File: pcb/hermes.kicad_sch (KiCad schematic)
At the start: 11 parts, among them J1 OLED_128x64, U1 XIAO-RP2040-DIP, U2 MAX30102

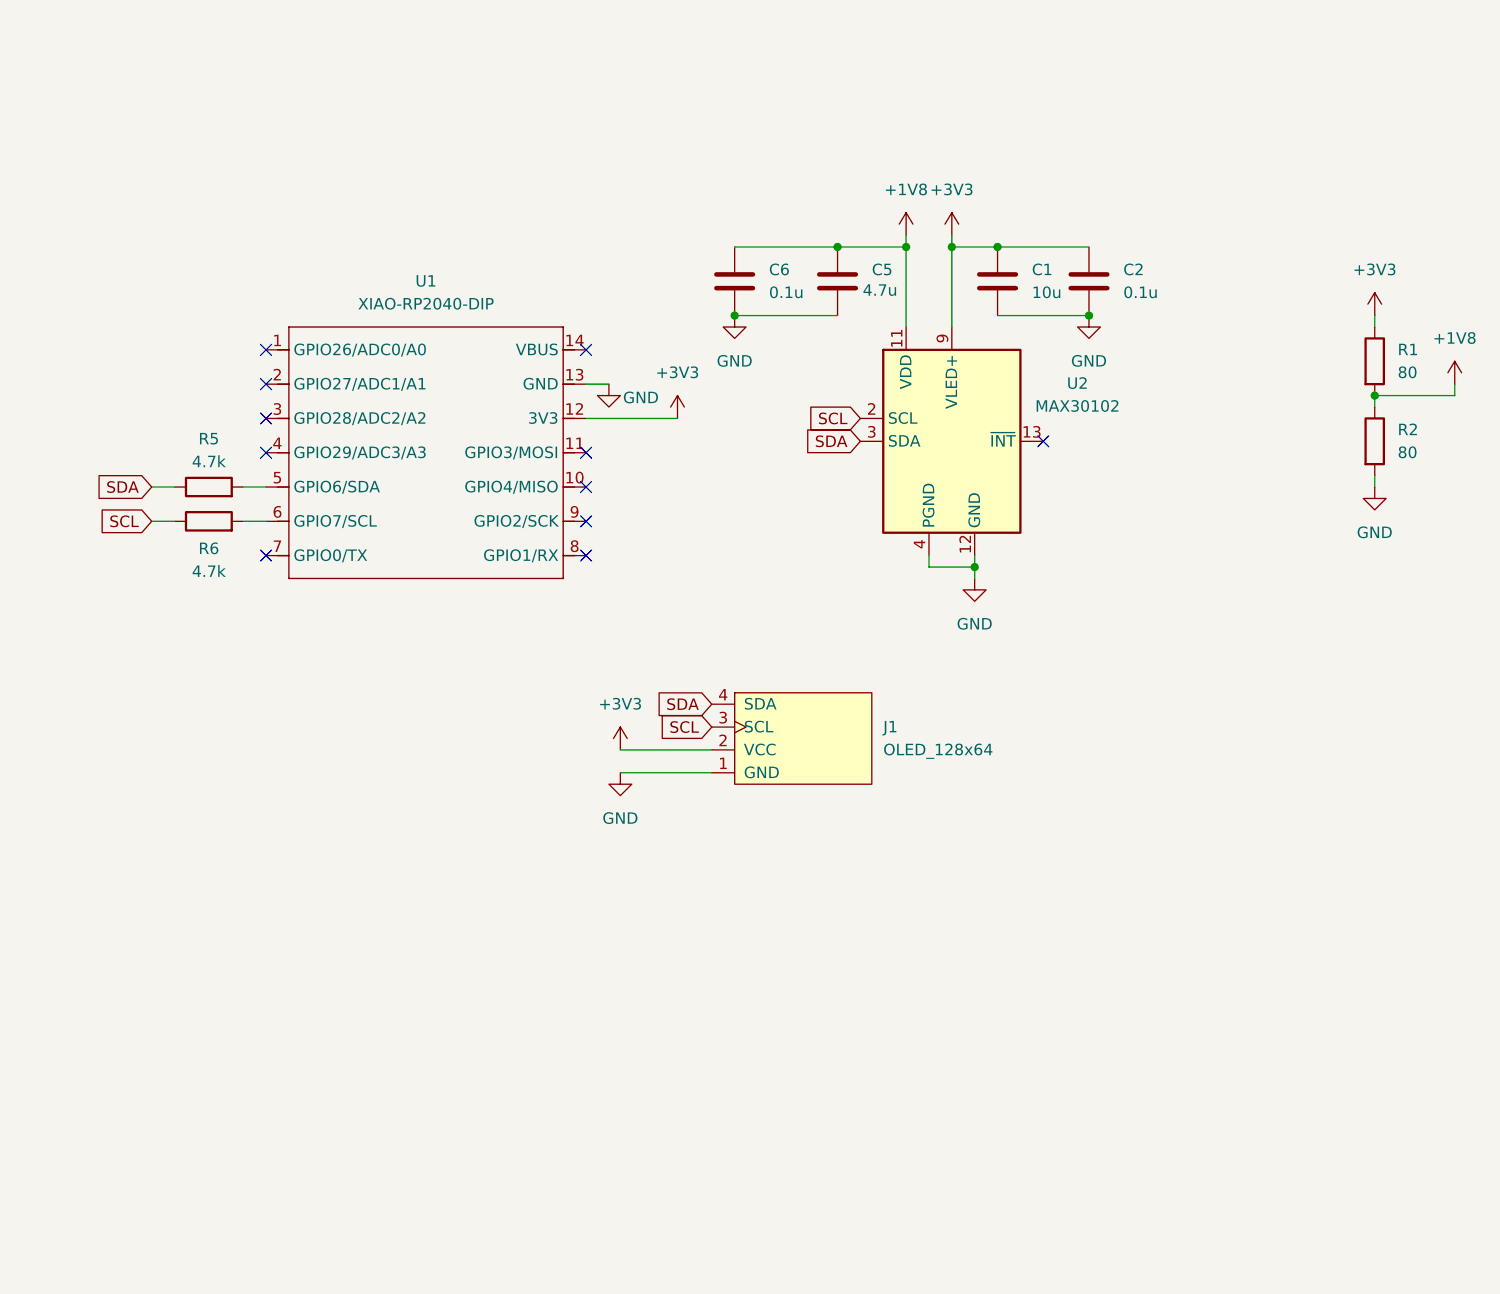
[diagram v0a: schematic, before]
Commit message: reroute board to incorporate TOF sensor
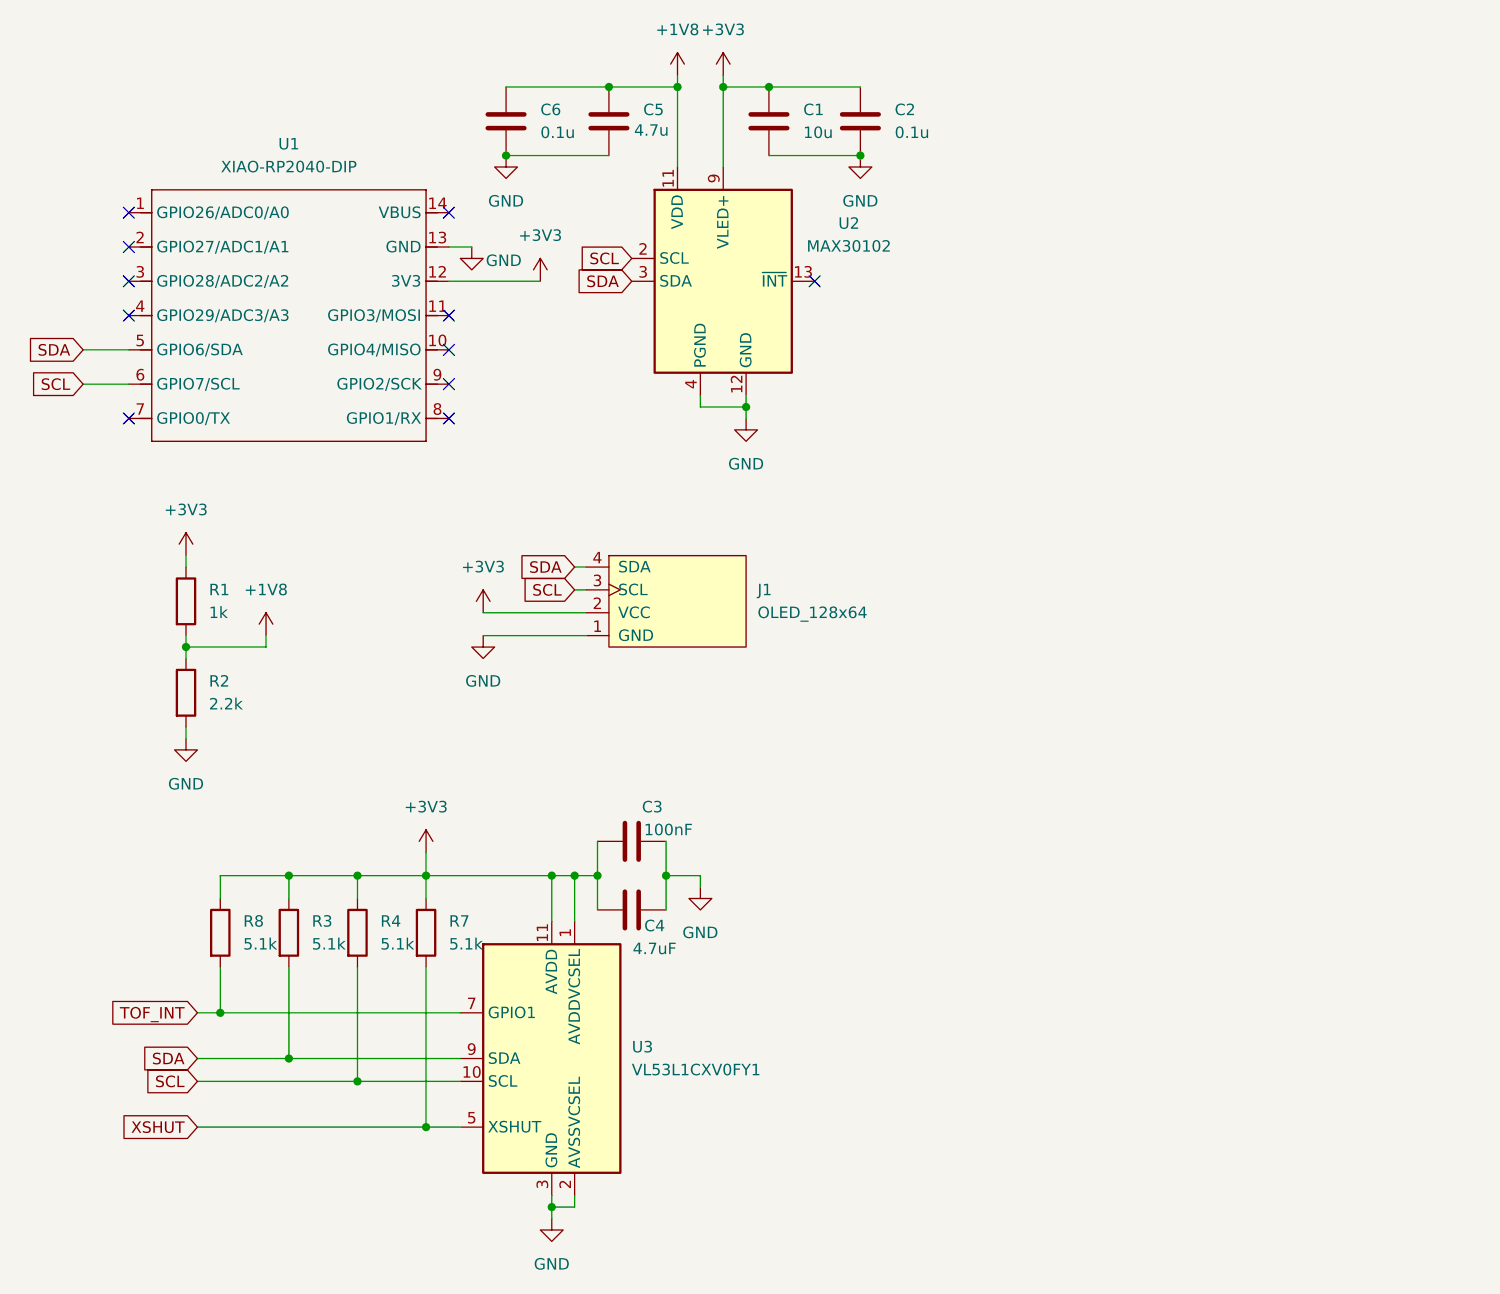
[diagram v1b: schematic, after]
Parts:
- removed R5, R6: 4.7k, Resistor_SMD:R_0805_2012Metric, symbol Device:R
- added C3: 100nF, Capacitor_SMD:C_0805_2012Metric, symbol Device:C
- added C4: 4.7uF, Capacitor_SMD:C_0805_2012Metric, symbol Device:C
- added R3, R4, R7, R8: 5.1k, Resistor_SMD:R_0805_2012Metric, symbol Device:R
- added U3: VL53L1CXV0FY1, Sensor_Distance:ST_VL53L1x, symbol Sensor_Distance:VL53L1CXV0FY1
- R1: value 80 -> 1k
- R2: value 80 -> 2.2k
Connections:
- net +3V3: now also C3.1, C4.1, R3.1, R4.1, R7.1, R8.1, U3.1 (AVDDVCSEL), U3.11 (AVDD)
- net GND: now also C3.2, C4.2, U3.12 (GND), U3.2 (AVSSVCSEL), U3.3 (GND), U3.4 (GND), U3.6 (GND)
- net SCL: now also U1.6 (GPIO7/SCL), R4.2, U3.10 (SCL)
- net SDA: now also U1.5 (GPIO6/SDA), R3.2, U3.9 (SDA)
- new net TOF_INT: R8.2, U3.7 (GPIO1)
- new net XSHUT: R7.2, U3.5 (XSHUT)
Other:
- moved on the sheet: C1, C2, C5, C6, J1, R1, R2, U1, U2
